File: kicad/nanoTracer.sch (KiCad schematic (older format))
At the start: 35 parts, among them J1 ARDUINO, T1 TRANSFO2, U2 ECC83, U3 LM833, U4 LM833

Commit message: Start modular Arduino shield project
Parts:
- removed C2: 220µ, ~, symbol CP1
- removed C?: 100n, ~, symbol C
- removed D1, D2, D3, D4: BAS70-04, diode-SOT23, symbol BAS70-04
- removed F?: FUSE, ~, symbol FUSE
- removed R12: 180R, ~, symbol R
- removed R3: 1R, ~, symbol R
- removed R?: 10k, ~, symbol R
- removed SW?: SW_PUSH, ~, symbol SW_PUSH
- removed T1: TRANSFO2, ~, symbol TRANSFO2
- removed U2, U? (x2): ECC83, VALVE-NOVAL_P, symbol ECC83
- removed U3, U4, U?: LM833, symbol TL082
- added C10, C12, C13, C14, C15, C4, C5, C8, C9: 100n, symbol C
- added C11: 100n, ~, symbol C-RESCUE-nanoTracer
- added C6: 220µ, symbol CP1
- added C7: 100µ, symbol CP1
- added D1, D3: B80C1500, symbol Diode_Bridge
- added D2: B380C1500, symbol Diode_Bridge
- added F1, F2, F3: FUSE, ~, symbol FUSE
- added JP1, JP2: JUMPER3, symbol JUMPER3
- added P1: 6.3_AC, symbol CONN_2-RESCUE-nanoTracer
- added P3: CONN_3, symbol CONN_3
- added P4: HT_AC, symbol CONN_2-RESCUE-nanoTracer
- added P5: NEG_AC, symbol CONN_2-RESCUE-nanoTracer
- added R15: 2.4k, ~, symbol R-RESCUE-nanoTracer
- added R16: 120R, ~, symbol R-RESCUE-nanoTracer
- added R8, R9: 100k, ~, symbol R-RESCUE-nanoTracer
- added U1: TL072, symbol TL072
- added U2: TL071, symbol TL071
- added U3: MCP4921-E/P, symbol MCP4921-E/P
- added U4: LM337T, TO-220, symbol LM337T
- added U5: MCP3202, symbol MCP3002
- added U6: SIL12, symbol SIL12
- C1: footprint ~ -> (none)
- C2: renamed from C3; value 47n -> 100n; symbol C -> C-RESCUE-nanoTracer
- C3: renamed from C4; value 82n -> 100n; symbol C -> C-RESCUE-nanoTracer
- J1: value ARDUINO -> ARDUINO_UNO_REV3_PINS
- P2: renamed from P?; value CONN_2 -> HEATER; symbol CONN_2 -> CONN_2-RESCUE-nanoTracer
- R1: renamed from R4; symbol R -> R-RESCUE-nanoTracer
- R10: renamed from R1; symbol R -> R-RESCUE-nanoTracer
- R11: renamed from R2; value 2.2k -> R; symbol R -> R-RESCUE-nanoTracer
- R12: renamed from R9; value 10k -> 1R; symbol R -> R-RESCUE-nanoTracer
- R13: renamed from R10; symbol R -> R-RESCUE-nanoTracer
- R14: renamed from R11; value 100k -> 10k; symbol R -> R-RESCUE-nanoTracer
- R2: renamed from R?; value 10k -> R; symbol R -> R-RESCUE-nanoTracer
- R3: renamed from R?; value 4.7k -> R; symbol R -> R-RESCUE-nanoTracer
- R4: renamed from R5; value 2k -> R; symbol R -> R-RESCUE-nanoTracer
- R5: renamed from R6; symbol R -> R-RESCUE-nanoTracer
- R6: renamed from R7; symbol R -> R-RESCUE-nanoTracer
- R7: renamed from R8; symbol R -> R-RESCUE-nanoTracer
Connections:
- net labels added: A+, BTN_DN, BTN_OK, BTN_UP, CS_ADC, CS_DAC, DAC_OUT, GRID, IA, LCD_D4, LCD_D5, LCD_D6, LCD_D7, LCD_EN, LCD_RS, MISO, MOSI, PWM_OUT, SCK, UA, UG, UK, VDD, VIN, VSS
- net labels removed: +5V, -5V, HT
- wire segments 96 -> 149
- no-connect marks 27 -> 10
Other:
- note added: "1.5k"
- note added: "12k"
- note added: "15k"
- note added: "2.2k"
- note added: "3.3V"
- note added: "5.1k"
- note added: "5V"
- note added: "8.2k"
- note added: "82k"
- note added: "91k"
- note added: "FITTED ONLY IF U3 IS PRESENT"
- note added: "IOREF"
- note added: "NOT FITTED IF NEG_AC IS PRESENT"
- note added: "NOT FITTED IF U3 IS PRESENT"
- note added: "OPTIONAL"
- note added: "R11"
- note added: "R2"
- note added: "R3"
- note added: "R4"
- note added: "WARNING: R2, R3, R4 & R11 VALUES\nDEPEND ON IOREF VOLTAGE\n\nARDUINO UNO HAS 5V IOREF\nARDUINO ZERO HAS 3.3V IOREF"
- moved on the sheet: C2, C3, P2

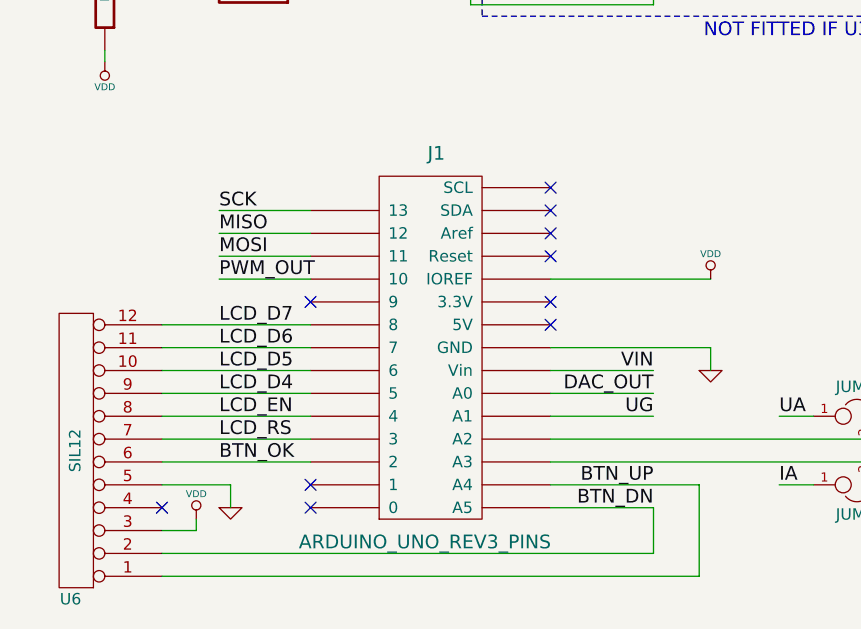
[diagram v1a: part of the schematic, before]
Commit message: Use SCL/SDA pins for buttons to ease routing
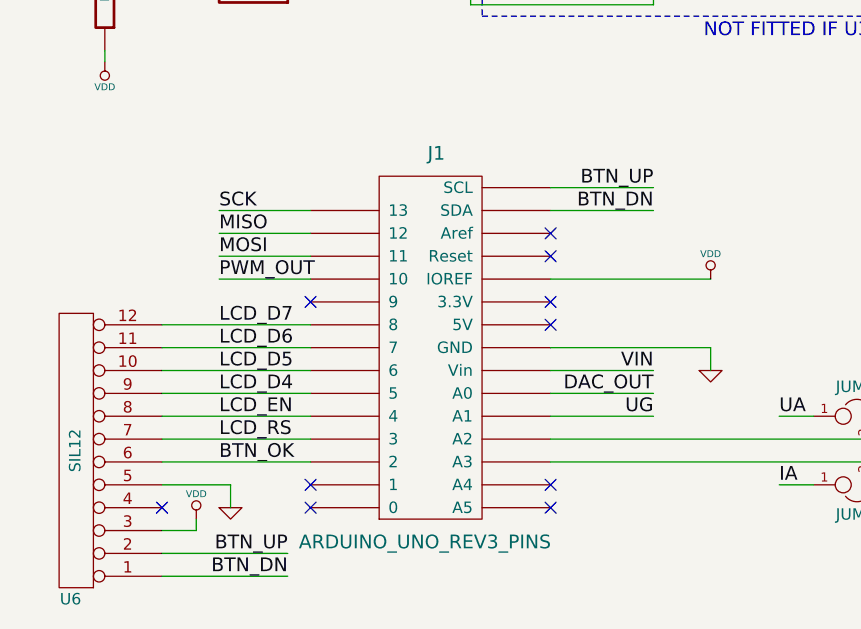
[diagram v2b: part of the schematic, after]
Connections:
- net BTN_DN: now also J1.SDA, U6.1; no longer J1.A5, U6.2
- net BTN_UP: now also J1.SCL, U6.2; no longer J1.A4, U6.1
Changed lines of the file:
@@
 	-1   0    0    -1
 $EndComp
-NoConn ~ 4100 5850
 NoConn ~ 4100 5950
 NoConn ~ 4100 6050
@@
 	2900 1150 2700 1150
 NoConn ~ 4100 6350
-$Comp
-L ARDUINO_UNO_REV3_PINS J1
-U 1 1 578E9E85
-P 3600 6450
-F 0 "J1" H 3600 7300 60  0000 C CNN
-F 1 "ARDUINO_UNO_REV3_PINS" H 3650 5600 60  0000 C CNN
-F 2 "" H 3600 6450 60  0000 C CNN
-F 3 "" H 3600 6450 60  0000 C CNN
-	1    3600 6450
-	-1   0    0    -1
-$EndComp
 Wire Wire Line
 	4100 6150 4800 6150
@@
 Text Label 8750 3150 0    60   ~ 0
 IA
-Text Label 4550 7050 2    60   ~ 0
+Text Label 4550 5750 2    60   ~ 0
 BTN_UP
-Text Label 4550 7150 2    60   ~ 0
+Text Label 4550 5850 2    60   ~ 0
 BTN_DN
 Text Label 5100 6750 0    60   ~ 0
@@
 	4100 6950 5500 6950
 Wire Wire Line
-	4100 7050 4750 7050
-Wire Wire Line
-	4550 7150 4100 7150
-Wire Wire Line
 	4550 6750 4100 6750
 Wire Wire Line
 	4100 6650 4550 6650
-NoConn ~ 4100 5750
 Text Label 2650 6950 0    60   ~ 0
 BTN_OK
@@
 	-1   0    0    1
 $EndComp
-Wire Wire Line
-	2400 7450 4750 7450
-Wire Wire Line
-	4750 7450 4750 7050
-Wire Wire Line
-	4550 7150 4550 7350
-Wire Wire Line
-	4550 7350 2400 7350
 $Comp
 L GND #PWR034
@@
 	2700 7050 2700 7150
 NoConn ~ 2400 7150
+$Comp
+L ARDUINO_UNO_REV3_PINS J1
+U 1 1 578E9E85
+P 3600 6450
+F 0 "J1" H 3600 7300 60  0000 C CNN
+F 1 "ARDUINO_UNO_REV3_PINS" H 3650 5600 60  0000 C CNN
+F 2 "" H 3600 6450 60  0000 C CNN
+F 3 "" H 3600 6450 60  0000 C CNN
+	1    3600 6450
+	-1   0    0    -1
+$EndComp
+Wire Wire Line
+	4100 5850 4550 5850
+Wire Wire Line
+	4550 5750 4100 5750
+Text Label 2950 7350 2    60   ~ 0
+BTN_UP
+Text Label 2950 7450 2    60   ~ 0
+BTN_DN
+Wire Wire Line
+	2400 7350 2950 7350
+Wire Wire Line
+	2400 7450 2950 7450
+NoConn ~ 4100 7050
+NoConn ~ 4100 7150
 $EndSCHEMATC

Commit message: Complete footprints association
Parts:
- removed J1: ARDUINO_UNO_REV3_PINS, symbol ARDUINO_UNO_REV3_PINS
- added SHIELD1: ARDUINO_SHIELD, freetronics_footprints:ARDUINO_SHIELD, symbol ARDUINO_SHIELD
- C1: footprint (none) -> Capacitors_ThroughHole:C_Radial_D10_L16_P5
- C10, C12, C13, C14, C15, C4, C5, C8, C9: footprint (none) -> Capacitors_ThroughHole:C_Rect_L7_W2_P5
- C11, C2, C3: footprint ~ -> Capacitors_ThroughHole:C_Rect_L7_W2_P5
- C6: footprint (none) -> Capacitors_ThroughHole:C_Radial_D7.5_L11.2_P2.5
- C7: footprint (none) -> Capacitors_ThroughHole:C_Radial_D6.3_L11.2_P2.5
- D1, D2, D3: footprint (none) -> w_pth_diodes:bridge_wob
- F1, F2, F3: footprint ~ -> Fuse_Holders_and_Fuses:Fuseholder5x20_horiz_open_Schurter_0031_8201
- JP1, JP2: footprint (none) -> Pin_Headers:Pin_Header_Straight_1x03
- P1, P2, P4, P5: footprint (none) -> Connect:bornier2
- P3: footprint (none) -> Connect:bornier3
- R1, R10, R11, R12, R13, R14, R15, R16, R2, R3, R4, R5, R6, R7, R8, R9: footprint ~ -> Resistors_ThroughHole:Resistor_Horizontal_RM10mm
- U1, U2, U3, U5: footprint (none) -> Housings_DIP:DIP-8_W7.62mm_LongPads
- U4: footprint TO-220 -> TO_SOT_Packages_THT:TO-220_Neutral123_Vertical
- U6: footprint (none) -> Pin_Headers:Pin_Header_Straight_1x12
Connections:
- net BTN_DN: now also SHIELD1.SDA
- net BTN_OK: now also SHIELD1.2
- net BTN_UP: now also SHIELD1.SCL
- net DAC_OUT: now also SHIELD1.AD0
- net GND: now also SHIELD1.GND1, SHIELD1.GND2
- net LCD_D4: now also SHIELD1.5
- net LCD_D5: now also SHIELD1.6
- net LCD_D6: now also SHIELD1.7
- net LCD_D7: now also SHIELD1.8
- net LCD_EN: now also SHIELD1.4
- net LCD_RS: now also SHIELD1.3
- net MISO: now also SHIELD1.12
- net MOSI: now also SHIELD1.11
- net PWM_OUT: now also SHIELD1.10
- net SCK: now also SHIELD1.13
- net UG: now also SHIELD1.AD1
- net VDD: now also SHIELD1.IO_R (IOREF)
- net VIN: now also SHIELD1.V_IN
- net at JP1.2: now also SHIELD1.AD2
- net at JP2.2: now also SHIELD1.AD3
- no-connect marks 10 -> 16
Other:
- moved on the sheet: C10, C11, C12, C13, C14, C15, C2, C3, C8, C9, JP1, JP2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
